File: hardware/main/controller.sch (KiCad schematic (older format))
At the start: 7 parts

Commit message: TO-DO List criada na folha principal
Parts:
- gave numbers to parts that had none: 7
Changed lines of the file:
@@
 P 6850 4700
 AR Path="/5CA5A5EB" Ref="#PWR?"  Part="1"
-AR Path="/5CA4DC1F/5CA5A5EB" Ref="#PWR?"  Part="1"
-F 0 "#PWR?" H 6850 4450 50  0001 C CNN
+AR Path="/5CA4DC1F/5CA5A5EB" Ref="#PWR0103"  Part="1"
+F 0 "#PWR0103" H 6850 4450 50  0001 C CNN
 F 1 "GND" H 6900 4500 50  0000 C CNN
 F 2 "" H 6850 4700 50  0001 C CNN
@@
 P 6650 3850
 AR Path="/5CA5A5F1" Ref="#PWR?"  Part="1"
-AR Path="/5CA4DC1F/5CA5A5F1" Ref="#PWR?"  Part="1"
-F 0 "#PWR?" H 6650 3700 50  0001 C CNN
+AR Path="/5CA4DC1F/5CA5A5F1" Ref="#PWR0104"  Part="1"
+F 0 "#PWR0104" H 6650 3700 50  0001 C CNN
 F 1 "+5V" H 6700 4050 50  0000 C CNN
 F 2 "" H 6650 3850 50  0001 C CNN
@@
 P 3450 4450
 AR Path="/5CA5A5F7" Ref="#PWR?"  Part="1"
-AR Path="/5CA4DC1F/5CA5A5F7" Ref="#PWR?"  Part="1"
-F 0 "#PWR?" H 3450 4300 50  0001 C CNN
+AR Path="/5CA4DC1F/5CA5A5F7" Ref="#PWR0105"  Part="1"
+F 0 "#PWR0105" H 3450 4300 50  0001 C CNN
 F 1 "+5V" H 3500 4650 50  0000 C CNN
 F 2 "" H 3450 4450 50  0001 C CNN
@@
 P 3450 4800
 AR Path="/5CA5A5FF" Ref="#PWR?"  Part="1"
-AR Path="/5CA4DC1F/5CA5A5FF" Ref="#PWR?"  Part="1"
-F 0 "#PWR?" H 3450 4550 50  0001 C CNN
+AR Path="/5CA4DC1F/5CA5A5FF" Ref="#PWR0106"  Part="1"
+F 0 "#PWR0106" H 3450 4550 50  0001 C CNN
 F 1 "GND" H 3500 4600 50  0000 C CNN
 F 2 "" H 3450 4800 50  0001 C CNN
@@
 P 2450 5000
 AR Path="/5CA5A626" Ref="#PWR?"  Part="1"
-AR Path="/5CA4DC1F/5CA5A626" Ref="#PWR?"  Part="1"
-F 0 "#PWR?" H 2450 4850 50  0001 C CNN
+AR Path="/5CA4DC1F/5CA5A626" Ref="#PWR0107"  Part="1"
+F 0 "#PWR0107" H 2450 4850 50  0001 C CNN
 F 1 "+5V" H 2500 5200 50  0000 C CNN
 F 2 "" H 2450 5000 50  0001 C CNN
@@
 P 2450 5150
 AR Path="/5CA5A62D" Ref="JP?"  Part="1"
-AR Path="/5CA4DC1F/5CA5A62D" Ref="JP?"  Part="1"
-F 0 "JP?" V 2404 5224 50  0000 L CNN
+AR Path="/5CA4DC1F/5CA5A62D" Ref="JP301"  Part="1"
+F 0 "JP301" V 2404 5224 50  0000 L CNN
 F 1 "Jp_TEST" V 2495 5224 50  0000 L CNN
 F 2 "" H 2450 5150 50  0001 C CNN
@@
 P 1450 5450
 AR Path="/5CA5A635" Ref="#PWR?"  Part="1"
-AR Path="/5CA4DC1F/5CA5A635" Ref="#PWR?"  Part="1"
-F 0 "#PWR?" H 1450 5200 50  0001 C CNN
+AR Path="/5CA4DC1F/5CA5A635" Ref="#PWR0112"  Part="1"
+F 0 "#PWR0112" H 1450 5200 50  0001 C CNN
 F 1 "GNDA" H 1455 5277 50  0000 C CNN
 F 2 "" H 1450 5450 50  0001 C CNN
@@
 P 1450 5700
 AR Path="/5CA5A63C" Ref="#PWR?"  Part="1"
-AR Path="/5CA4DC1F/5CA5A63C" Ref="#PWR?"  Part="1"
-F 0 "#PWR?" H 1450 5450 50  0001 C CNN
+AR Path="/5CA4DC1F/5CA5A63C" Ref="#PWR0113"  Part="1"
+F 0 "#PWR0113" H 1450 5450 50  0001 C CNN
 F 1 "GNDA" H 1455 5527 50  0000 C CNN
 F 2 "" H 1450 5700 50  0001 C CNN
@@
 P 1450 5350
 AR Path="/5CA5A645" Ref="JP?"  Part="1"
-AR Path="/5CA4DC1F/5CA5A645" Ref="JP?"  Part="1"
-F 0 "JP?" H 1450 5562 50  0001 C CNN
+AR Path="/5CA4DC1F/5CA5A645" Ref="JP302"  Part="1"
+F 0 "JP302" H 1450 5562 50  0001 C CNN
 F 1 "Jp_TEST" H 1450 5471 50  0001 C CNN
 F 2 "" H 1450 5350 50  0001 C CNN
@@
 P 1450 5600
 AR Path="/5CA5A64D" Ref="JP?"  Part="1"
-AR Path="/5CA4DC1F/5CA5A64D" Ref="JP?"  Part="1"
-F 0 "JP?" H 1450 5812 50  0001 C CNN
+AR Path="/5CA4DC1F/5CA5A64D" Ref="JP303"  Part="1"
+F 0 "JP303" H 1450 5812 50  0001 C CNN
 F 1 "Jp_TEST" H 1450 5721 50  0001 C CNN
 F 2 "" H 1450 5600 50  0001 C CNN
@@
 P 2450 6150
 AR Path="/5CA5A655" Ref="#PWR?"  Part="1"
-AR Path="/5CA4DC1F/5CA5A655" Ref="#PWR?"  Part="1"
-F 0 "#PWR?" H 2450 5900 50  0001 C CNN
+AR Path="/5CA4DC1F/5CA5A655" Ref="#PWR0114"  Part="1"
+F 0 "#PWR0114" H 2450 5900 50  0001 C CNN
 F 1 "GND" H 2500 5950 50  0000 C CNN
 F 2 "" H 2450 6150 50  0001 C CNN
@@
 P 2400 3150
 AR Path="/5CA5D716" Ref="H?"  Part="1"
-AR Path="/5CA4DC1F/5CA5D716" Ref="H?"  Part="1"
-F 0 "H?" H 2500 3200 50  0000 L CNN
+AR Path="/5CA4DC1F/5CA5D716" Ref="H304"  Part="1"
+F 0 "H304" H 2500 3200 50  0000 L CNN
 F 1 "MountingHole" H 2500 3150 50  0000 L CNN
 F 2 "MountingHole:MountingHole_3.2mm_M3" H 2400 3150 50  0001 C CNN
@@
 P 2400 2950
 AR Path="/5CA5D71C" Ref="H?"  Part="1"
-AR Path="/5CA4DC1F/5CA5D71C" Ref="H?"  Part="1"
-F 0 "H?" H 2500 3000 50  0000 L CNN
+AR Path="/5CA4DC1F/5CA5D71C" Ref="H303"  Part="1"
+F 0 "H303" H 2500 3000 50  0000 L CNN
 F 1 "MountingHole" H 2500 2950 50  0000 L CNN
 F 2 "MountingHole:MountingHole_3.2mm_M3" H 2400 2950 50  0001 C CNN
@@
 P 2400 2750
 AR Path="/5CA5D722" Ref="H?"  Part="1"
-AR Path="/5CA4DC1F/5CA5D722" Ref="H?"  Part="1"
-F 0 "H?" H 2500 2800 50  0000 L CNN
+AR Path="/5CA4DC1F/5CA5D722" Ref="H302"  Part="1"
+F 0 "H302" H 2500 2800 50  0000 L CNN
 F 1 "MountingHole" H 2500 2750 50  0000 L CNN
 F 2 "MountingHole:MountingHole_3.2mm_M3" H 2400 2750 50  0001 C CNN
@@
 P 2400 2550
 AR Path="/5CA5D728" Ref="H?"  Part="1"
-AR Path="/5CA4DC1F/5CA5D728" Ref="H?"  Part="1"
-F 0 "H?" H 2500 2600 50  0000 L CNN
+AR Path="/5CA4DC1F/5CA5D728" Ref="H301"  Part="1"
+F 0 "H301" H 2500 2600 50  0000 L CNN
 F 1 "MountingHole" H 2500 2550 50  0000 L CNN
 F 2 "MountingHole:MountingHole_3.2mm_M3" H 2400 2550 50  0001 C CNN

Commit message: Alimentação de 12V criada no Charger, que recebe 18V do Controller
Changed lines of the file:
@@
 Connection ~ 8450 3300
 Wire Wire Line
-	8450 3300 8050 3300
+	8450 3300 8250 3300
 Wire Wire Line
 	10150 3300 9900 3300
@@
 Wire Wire Line
 	2450 6050 2450 5750
+Text HLabel 8050 2900 0    50   Input ~ 0
++18V_OUT
+Wire Wire Line
+	8050 2900 8250 2900
+Wire Wire Line
+	8250 2900 8250 3300
+Connection ~ 8250 3300
+Wire Wire Line
+	8250 3300 8050 3300
 $EndSCHEMATC

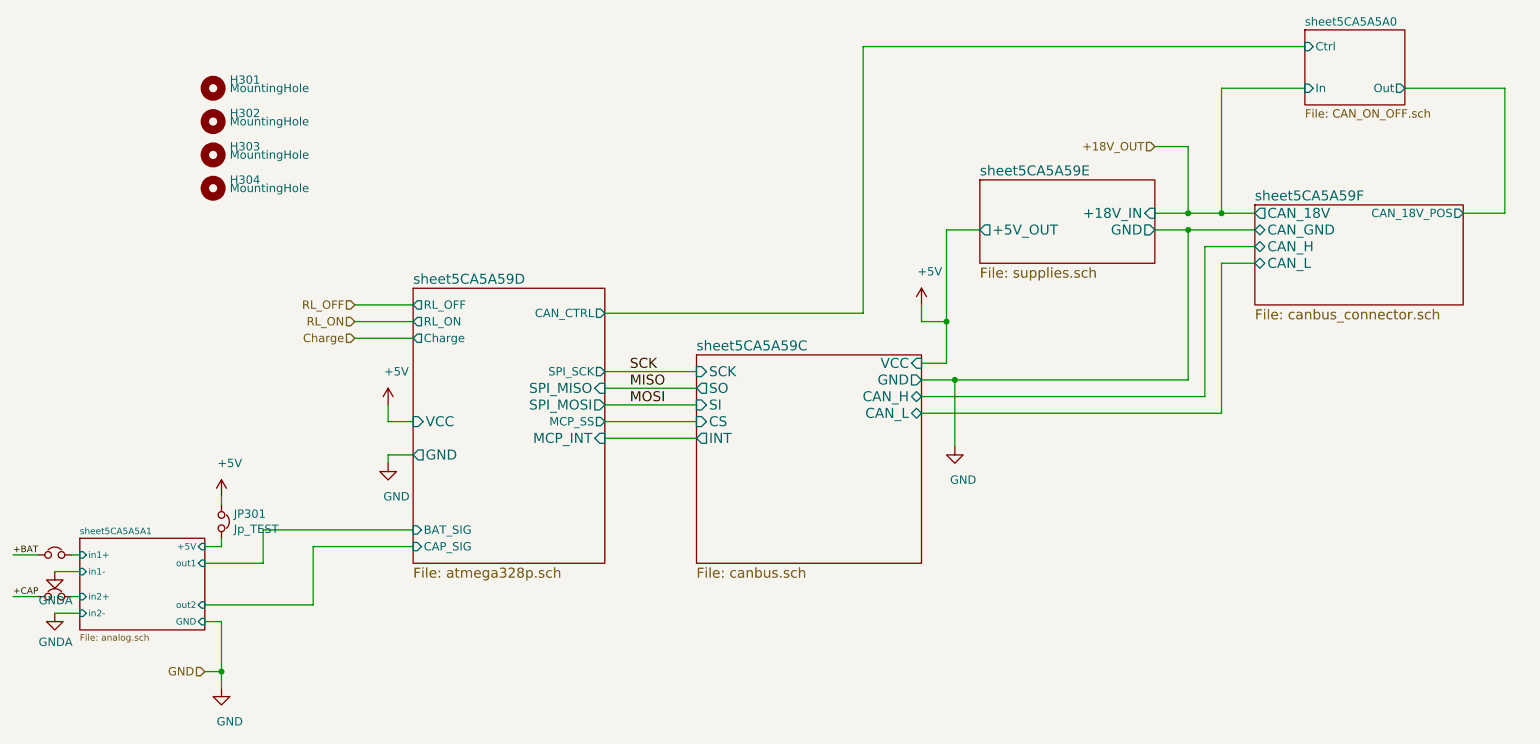
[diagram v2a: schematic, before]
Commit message: CAN CTRL_D / CAN_ON_OFF removidos.
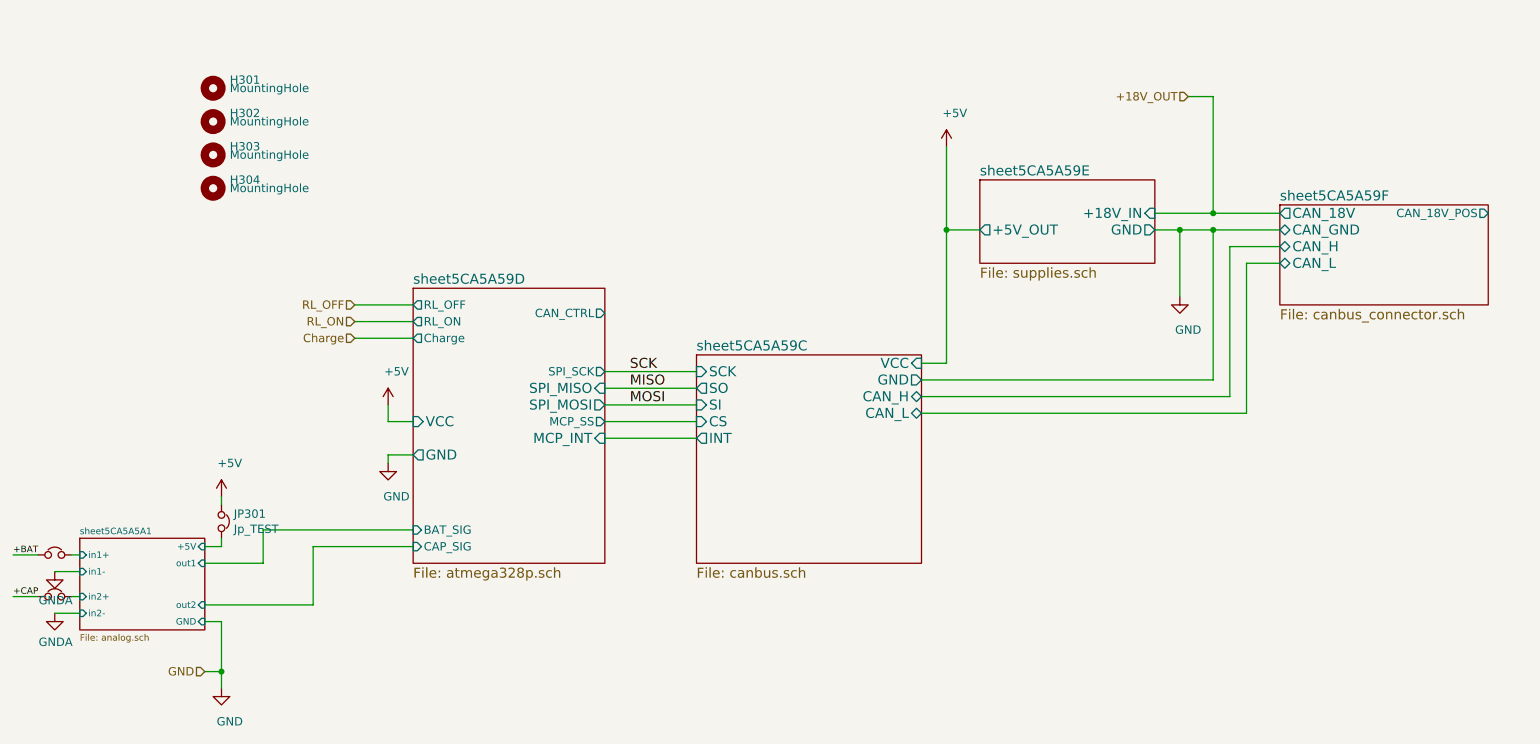
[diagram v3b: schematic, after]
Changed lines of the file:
@@
 $Descr A4 11693 8268
 encoding utf-8
-Sheet 3 9
+Sheet 3 8
 Title ""
 Date ""
@@
 $EndSheet
 $Sheet
-S 8650 3250 1250 600
+S 8800 3250 1250 600
 U 5CA5A5C7
 F0 "sheet5CA5A59F" 60
 F1 "canbus_connector.sch" 60
-F2 "CAN_H" B L 8650 3500 60
-F3 "CAN_L" B L 8650 3600 60
-F4 "CAN_18V" O L 8650 3300 60
-F5 "CAN_GND" B L 8650 3400 60
-F6 "CAN_18V_POS" O R 9900 3300 50
+F2 "CAN_H" B L 8800 3500 60
+F3 "CAN_L" B L 8800 3600 60
+F4 "CAN_18V" O L 8800 3300 60
+F5 "CAN_GND" B L 8800 3400 60
+F6 "CAN_18V_POS" O R 10050 3300 50
 $EndSheet
 Wire Wire Line
@@
 SCK
 Wire Wire Line
-	8650 3300 8450 3300
-Wire Wire Line
-	8050 3400 8250 3400
-Wire Wire Line
-	8650 3500 8350 3500
-Wire Wire Line
-	8350 3500 8350 4400
-Wire Wire Line
-	8350 4400 6650 4400
-Wire Wire Line
-	6650 4500 8450 4500
-Wire Wire Line
-	8450 4500 8450 3600
-Wire Wire Line
-	8450 3600 8650 3600
-Wire Wire Line
-	8250 3400 8250 4300
-Wire Wire Line
-	8250 4300 6850 4300
-Connection ~ 8250 3400
+	8050 3400 8200 3400
+Wire Wire Line
+	8800 3500 8500 3500
+Wire Wire Line
+	8500 3500 8500 4400
+Wire Wire Line
+	8500 4400 6650 4400
+Wire Wire Line
+	6650 4500 8600 4500
+Wire Wire Line
+	8600 4500 8600 3600
+Wire Wire Line
+	8600 3600 8800 3600
+Wire Wire Line
+	8400 3400 8400 4300
+Connection ~ 8400 3400
 Wire Wire Line
 	7000 3400 6800 3400
 Wire Wire Line
-	6800 3400 6800 3950
-Wire Wire Line
 	6800 4200 6650 4200
 Wire Wire Line
-	6850 4300 6850 4700
-Connection ~ 6850 4300
-Wire Wire Line
-	6850 4300 6650 4300
-Wire Wire Line
-	6650 3850 6650 3950
-Wire Wire Line
-	6650 3950 6800 3950
-Connection ~ 6800 3950
-Wire Wire Line
-	6800 3950 6800 4200
-Wire Wire Line
-	8250 3400 8650 3400
+	8200 3400 8200 3800
+Wire Wire Line
+	8400 3400 8800 3400
 $Comp
 L power:GND #PWR?
 U 1 1 5CA5A5EB
-P 6850 4700
+P 8200 3800
 AR Path="/5CA5A5EB" Ref="#PWR?"  Part="1"
 AR Path="/5CA4DC1F/5CA5A5EB" Ref="#PWR0103"  Part="1"
-F 0 "#PWR0103" H 6850 4450 50  0001 C CNN
-F 1 "GND" H 6900 4500 50  0000 C CNN
-F 2 "" H 6850 4700 50  0001 C CNN
-F 3 "" H 6850 4700 50  0001 C CNN
-	1    6850 4700
+F 0 "#PWR0103" H 8200 3550 50  0001 C CNN
+F 1 "GND" H 8250 3600 50  0000 C CNN
+F 2 "" H 8200 3800 50  0001 C CNN
+F 3 "" H 8200 3800 50  0001 C CNN
+	1    8200 3800
 	1    0    0    -1
 $EndComp
@@
 L power:+5V #PWR?
 U 1 1 5CA5A5F1
-P 6650 3850
+P 6800 2900
 AR Path="/5CA5A5F1" Ref="#PWR?"  Part="1"
 AR Path="/5CA4DC1F/5CA5A5F1" Ref="#PWR0104"  Part="1"
-F 0 "#PWR0104" H 6650 3700 50  0001 C CNN
-F 1 "+5V" H 6700 4050 50  0000 C CNN
-F 2 "" H 6650 3850 50  0001 C CNN
-F 3 "" H 6650 3850 50  0001 C CNN
-	1    6650 3850
+F 0 "#PWR0104" H 6800 2750 50  0001 C CNN
+F 1 "+5V" H 6850 3100 50  0000 C CNN
+F 2 "" H 6800 2900 50  0001 C CNN
+F 3 "" H 6800 2900 50  0001 C CNN
+	1    6800 2900
 	1    0    0    -1
 $EndComp
@@
 Wire Wire Line
 	3450 4750 3600 4750
-$Sheet
-S 8950 2200 600  450
-U 5CA5A606
-F0 "sheet5CA5A5A0" 50
-F1 "CAN_ON_OFF.sch" 50
-F2 "In" I L 8950 2550 50
-F3 "Out" O R 9550 2550 50
-F4 "Ctrl" I L 8950 2300 50
-$EndSheet
-Connection ~ 8450 3300
-Wire Wire Line
-	8450 3300 8250 3300
-Wire Wire Line
-	10150 3300 9900 3300
-Wire Wire Line
-	8950 2550 8450 2550
-Wire Wire Line
-	8450 2550 8450 3300
-Wire Wire Line
-	9550 2550 10150 2550
-Wire Wire Line
-	10150 2550 10150 3300
-Wire Wire Line
-	4750 3900 6300 3900
-Wire Wire Line
-	6300 3900 6300 2300
-Wire Wire Line
-	6300 2300 8950 2300
 $Sheet
 S 1600 5250 750  550
@@
 Wire Wire Line
 	2450 6050 2450 5750
-Text HLabel 8050 2900 0    50   Input ~ 0
+Text HLabel 8250 2600 0    50   Input ~ 0
 +18V_OUT
 Wire Wire Line
-	8050 2900 8250 2900
-Wire Wire Line
-	8250 2900 8250 3300
-Connection ~ 8250 3300
-Wire Wire Line
-	8250 3300 8050 3300
+	8250 2600 8400 2600
+Wire Wire Line
+	8400 2600 8400 3300
+Connection ~ 8400 3300
+Wire Wire Line
+	8400 3300 8050 3300
+Wire Wire Line
+	8400 3300 8800 3300
+Wire Wire Line
+	6800 3400 6800 4200
+Connection ~ 8200 3400
+Wire Wire Line
+	8200 3400 8400 3400
+Wire Wire Line
+	6650 4300 8400 4300
+Wire Wire Line
+	6800 2900 6800 3400
+Connection ~ 6800 3400
 $EndSCHEMATC

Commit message: Analog passado para o Charger
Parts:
- removed JP301, JP302, JP303: Jp_TEST, symbol Device:Jumper_NC_Small
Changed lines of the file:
@@
 $Descr A4 11693 8268
 encoding utf-8
-Sheet 3 8
+Sheet 4 8
 Title ""
 Date ""
@@
 F7 "SPI_SCK" O R 4750 4250 50
 F8 "MCP_SS" O R 4750 4550 50
-F9 "CAN_CTRL" O R 4750 3900 50
 F10 "RL_OFF" O L 3600 3850 50
 F11 "RL_ON" O L 3600 3950 50
@@
 $EndSheet
 $Sheet
-S 8800 3250 1250 600
+S 8800 3250 1000 450
 U 5CA5A5C7
 F0 "sheet5CA5A59F" 60
@@
 F4 "CAN_18V" O L 8800 3300 60
 F5 "CAN_GND" B L 8800 3400 60
-F6 "CAN_18V_POS" O R 10050 3300 50
 $EndSheet
 Wire Wire Line
@@
 	6800 4200 6650 4200
 Wire Wire Line
-	8200 3400 8200 3800
+	8200 3400 8200 3850
 Wire Wire Line
 	8400 3400 8800 3400
@@
 L power:GND #PWR?
 U 1 1 5CA5A5EB
-P 8200 3800
+P 8200 3950
 AR Path="/5CA5A5EB" Ref="#PWR?"  Part="1"
 AR Path="/5CA4DC1F/5CA5A5EB" Ref="#PWR0103"  Part="1"
-F 0 "#PWR0103" H 8200 3550 50  0001 C CNN
-F 1 "GND" H 8250 3600 50  0000 C CNN
-F 2 "" H 8200 3800 50  0001 C CNN
-F 3 "" H 8200 3800 50  0001 C CNN
-	1    8200 3800
+F 0 "#PWR0103" H 8200 3700 50  0001 C CNN
+F 1 "GND" H 8250 3750 50  0000 C CNN
+F 2 "" H 8200 3950 50  0001 C CNN
+F 3 "" H 8200 3950 50  0001 C CNN
+	1    8200 3950
 	1    0    0    -1
 $EndComp
@@
 Wire Wire Line
 	3450 4750 3600 4750
-$Sheet
-S 1600 5250 750  550
-U 5CA5A61A
-F0 "sheet5CA5A5A1" 39
-F1 "analog.sch" 39
-F2 "out1" I R 2350 5400 39
-F3 "+5V" I R 2350 5300 39
-F4 "GND" I R 2350 5750 39
-F5 "in1-" I L 1600 5450 39
-F6 "in1+" I L 1600 5350 39
-F7 "out2" I R 2350 5650 39
-F8 "in2-" I L 1600 5700 39
-F9 "in2+" I L 1600 5600 39
-$EndSheet
-Wire Wire Line
-	2350 5650 3000 5650
-Wire Wire Line
-	3000 5650 3000 5300
 Wire Wire Line
 	3000 5300 3600 5300
-Wire Wire Line
-	2350 5400 2700 5400
-Wire Wire Line
-	2700 5400 2700 5200
-Wire Wire Line
-	2700 5200 3600 5200
-$Comp
-L power:+5V #PWR?
-U 1 1 5CA5A626
-P 2450 5000
-AR Path="/5CA5A626" Ref="#PWR?"  Part="1"
-AR Path="/5CA4DC1F/5CA5A626" Ref="#PWR0107"  Part="1"
-F 0 "#PWR0107" H 2450 4850 50  0001 C CNN
-F 1 "+5V" H 2500 5200 50  0000 C CNN
-F 2 "" H 2450 5000 50  0001 C CNN
-F 3 "" H 2450 5000 50  0001 C CNN
-	1    2450 5000
-	1    0    0    -1
-$EndComp
-Wire Wire Line
-	2450 5300 2350 5300
-$Comp
-L Device:Jumper_NC_Small JP?
-U 1 1 5CA5A62D
-P 2450 5150
-AR Path="/5CA5A62D" Ref="JP?"  Part="1"
-AR Path="/5CA4DC1F/5CA5A62D" Ref="JP301"  Part="1"
-F 0 "JP301" V 2404 5224 50  0000 L CNN
-F 1 "Jp_TEST" V 2495 5224 50  0000 L CNN
-F 2 "" H 2450 5150 50  0001 C CNN
-F 3 "~" H 2450 5150 50  0001 C CNN
-	1    2450 5150
-	0    1    1    0
-$EndComp
-Wire Wire Line
-	2450 5050 2450 5000
-Wire Wire Line
-	2450 5250 2450 5300
-$Comp
-L power:GNDA #PWR?
-U 1 1 5CA5A635
-P 1450 5450
-AR Path="/5CA5A635" Ref="#PWR?"  Part="1"
-AR Path="/5CA4DC1F/5CA5A635" Ref="#PWR0112"  Part="1"
-F 0 "#PWR0112" H 1450 5200 50  0001 C CNN
-F 1 "GNDA" H 1455 5277 50  0000 C CNN
-F 2 "" H 1450 5450 50  0001 C CNN
-F 3 "" H 1450 5450 50  0001 C CNN
-	1    1450 5450
-	1    0    0    -1
-$EndComp
-Wire Wire Line
-	1450 5450 1600 5450
-$Comp
-L power:GNDA #PWR?
-U 1 1 5CA5A63C
-P 1450 5700
-AR Path="/5CA5A63C" Ref="#PWR?"  Part="1"
-AR Path="/5CA4DC1F/5CA5A63C" Ref="#PWR0113"  Part="1"
-F 0 "#PWR0113" H 1450 5450 50  0001 C CNN
-F 1 "GNDA" H 1455 5527 50  0000 C CNN
-F 2 "" H 1450 5700 50  0001 C CNN
-F 3 "" H 1450 5700 50  0001 C CNN
-	1    1450 5700
-	1    0    0    -1
-$EndComp
-Wire Wire Line
-	1450 5700 1600 5700
-Text Label 1200 5600 0    39   ~ 0
-+CAP
-Text Label 1200 5350 0    39   ~ 0
-+BAT
-$Comp
-L Device:Jumper_NC_Small JP?
-U 1 1 5CA5A645
-P 1450 5350
-AR Path="/5CA5A645" Ref="JP?"  Part="1"
-AR Path="/5CA4DC1F/5CA5A645" Ref="JP302"  Part="1"
-F 0 "JP302" H 1450 5562 50  0001 C CNN
-F 1 "Jp_TEST" H 1450 5471 50  0001 C CNN
-F 2 "" H 1450 5350 50  0001 C CNN
-F 3 "~" H 1450 5350 50  0001 C CNN
-	1    1450 5350
-	1    0    0    -1
-$EndComp
-Wire Wire Line
-	1200 5350 1350 5350
-Wire Wire Line
-	1550 5350 1600 5350
-$Comp
-L Device:Jumper_NC_Small JP?
-U 1 1 5CA5A64D
-P 1450 5600
-AR Path="/5CA5A64D" Ref="JP?"  Part="1"
-AR Path="/5CA4DC1F/5CA5A64D" Ref="JP303"  Part="1"
-F 0 "JP303" H 1450 5812 50  0001 C CNN
-F 1 "Jp_TEST" H 1450 5721 50  0001 C CNN
-F 2 "" H 1450 5600 50  0001 C CNN
-F 3 "~" H 1450 5600 50  0001 C CNN
-	1    1450 5600
-	1    0    0    -1
-$EndComp
-Wire Wire Line
-	1200 5600 1350 5600
-Wire Wire Line
-	1550 5600 1600 5600
-$Comp
-L power:GND #PWR?
-U 1 1 5CA5A655
-P 2450 6150
-AR Path="/5CA5A655" Ref="#PWR?"  Part="1"
-AR Path="/5CA4DC1F/5CA5A655" Ref="#PWR0114"  Part="1"
-F 0 "#PWR0114" H 2450 5900 50  0001 C CNN
-F 1 "GND" H 2500 5950 50  0000 C CNN
-F 2 "" H 2450 6150 50  0001 C CNN
-F 3 "" H 2450 6150 50  0001 C CNN
-	1    2450 6150
-	1    0    0    -1
-$EndComp
-Wire Wire Line
-	2450 6150 2450 6050
-Wire Wire Line
-	2450 5750 2350 5750
 $Comp
 L Mechanical:MountingHole H?
@@
 Text HLabel 3250 4050 0    50   Input ~ 0
 Charge
-Text HLabel 2350 6050 0    50   Input ~ 0
-GND
-Wire Wire Line
-	2350 6050 2450 6050
-Connection ~ 2450 6050
-Wire Wire Line
-	2450 6050 2450 5750
 Text HLabel 8250 2600 0    50   Input ~ 0
 +18V_OUT
@@
 	6800 2900 6800 3400
 Connection ~ 6800 3400
+Wire Wire Line
+	3600 5200 3000 5200
+Text HLabel 3000 5200 0    50   Input ~ 0
+sig_bat+
+Text HLabel 3000 5300 0    50   Input ~ 0
+sig_cap+
+Text HLabel 8150 3850 0    50   Output ~ 0
+GND
+Wire Wire Line
+	8150 3850 8200 3850
+Connection ~ 8200 3850
+Wire Wire Line
+	8200 3850 8200 3950
 $EndSCHEMATC
